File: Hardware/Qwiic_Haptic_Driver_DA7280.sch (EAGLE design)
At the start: 23 parts, among them J1 QWIIC_RIGHT_ANGLE, J2 QWIIC_RIGHT_ANGLE, M1 G1040003D_LRA_CASTELLATED, U1 HAPTIC_DRIVER_DA7280

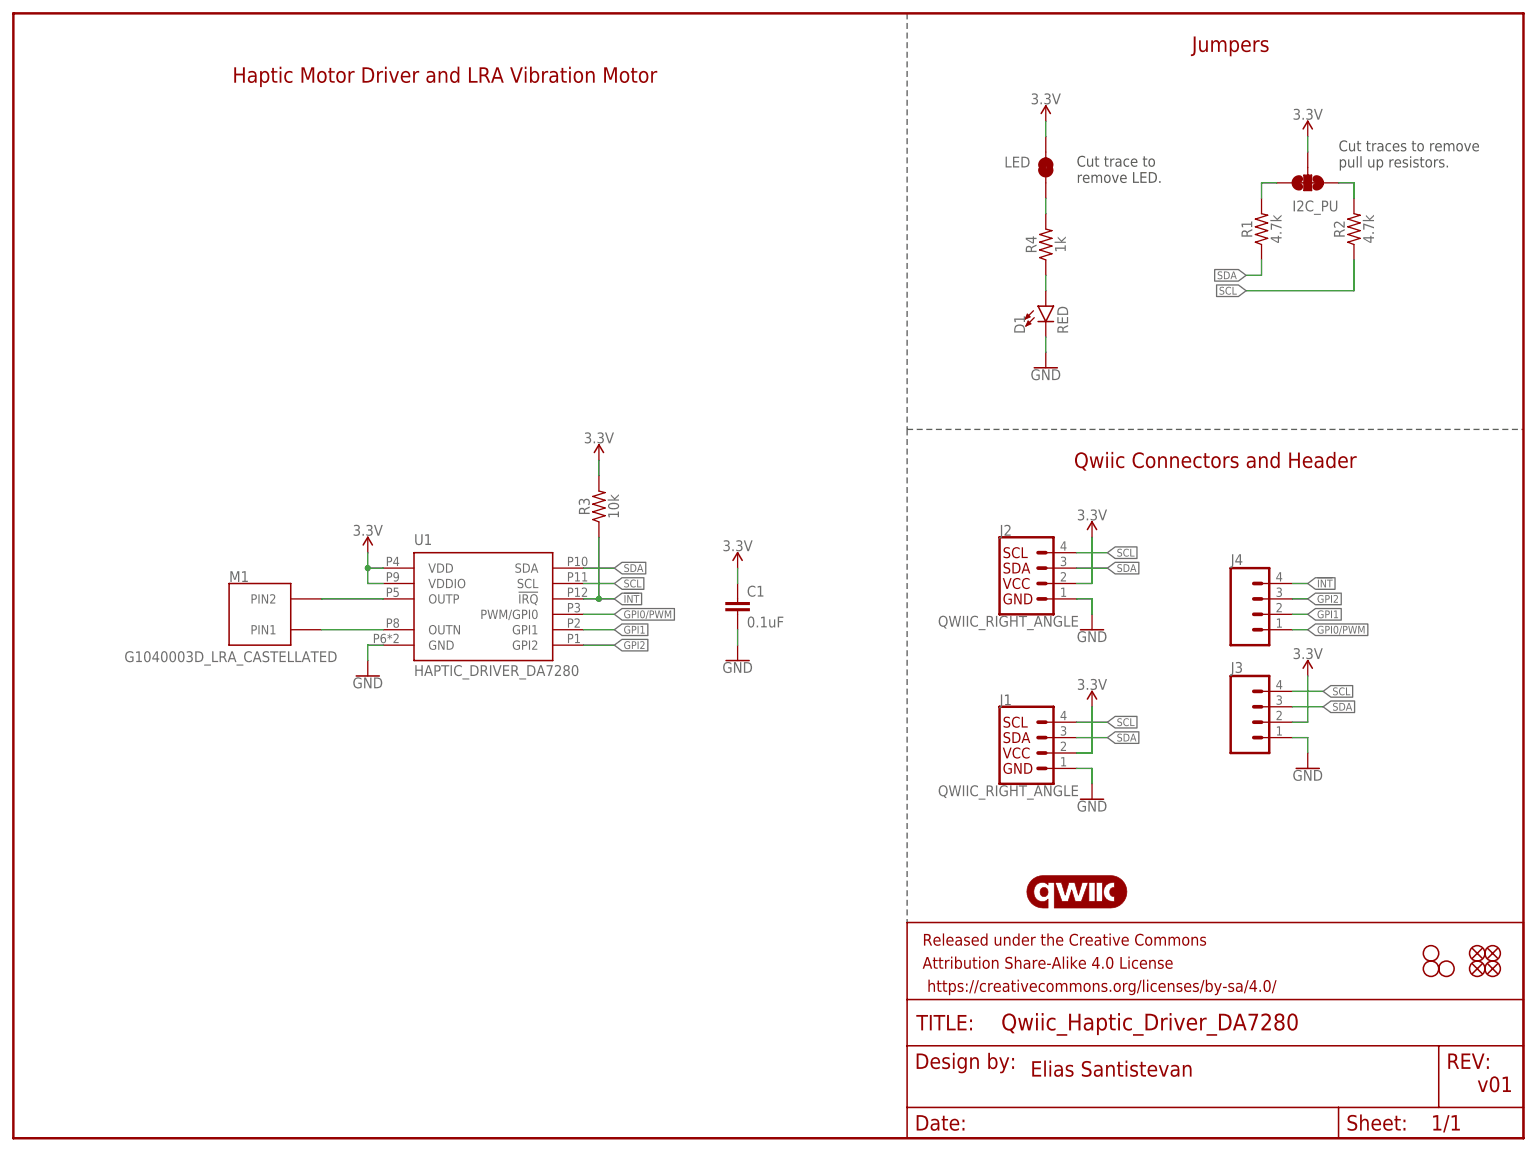
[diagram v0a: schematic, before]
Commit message: Flips the LRA motor 180, extends board to be 1.15 x 1 inches, adds 4.7iF decoupling capacitor
* Gerbers in repo are out of date
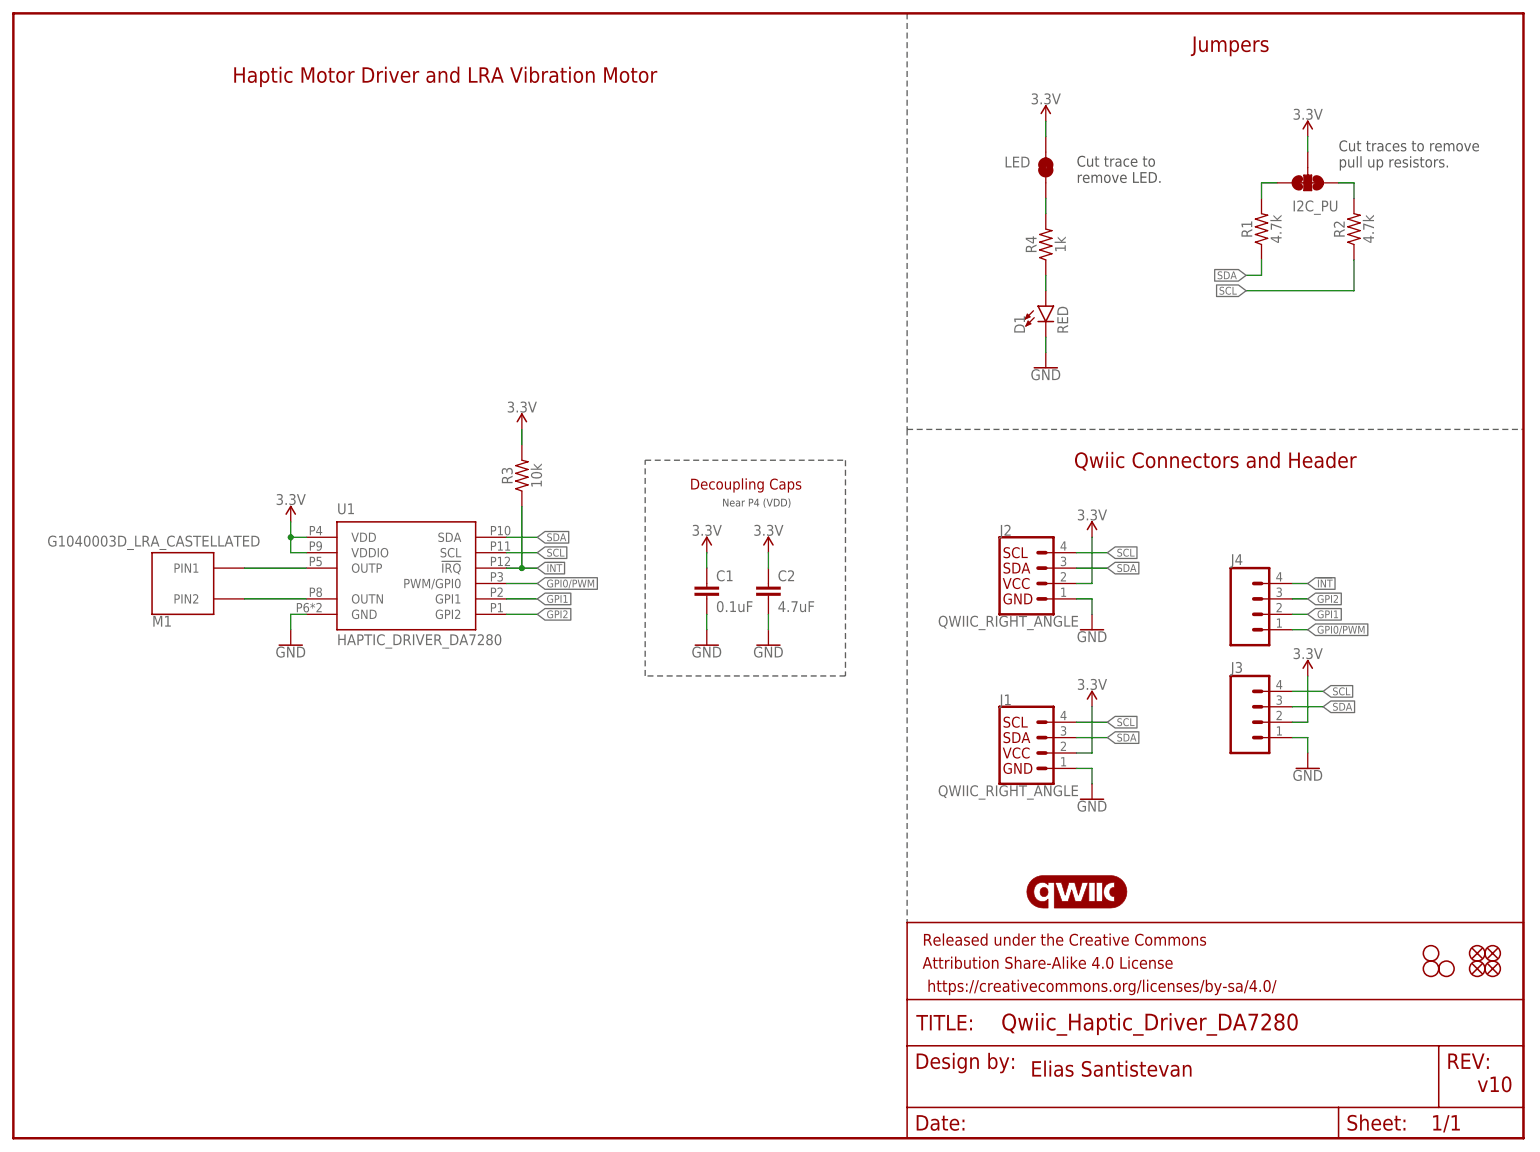
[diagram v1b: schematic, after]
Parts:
- added C2: 4.7uF, SparkFun-Capacitors:4.7UF-0603-6.3V-(10%)
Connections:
- net 3.3V: now also C2.1
- net GND: now also C2.2
- net N$5: now also U1.OUTP; no longer U1.OUTN
- net N$6: now also U1.OUTN; no longer U1.OUTP
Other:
- note added: "Decoupling Caps"
- note added: "Near P4 (VDD)"
- note added: "v10"
- note removed: "v01"
- moved on the sheet: C1, M1, R3, U1

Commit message: Adds a jumper and plated through hole for separate VDDIO supply, adds silk for VDD
* Changes power symbols to VDD and VDDIO in place of 3V3
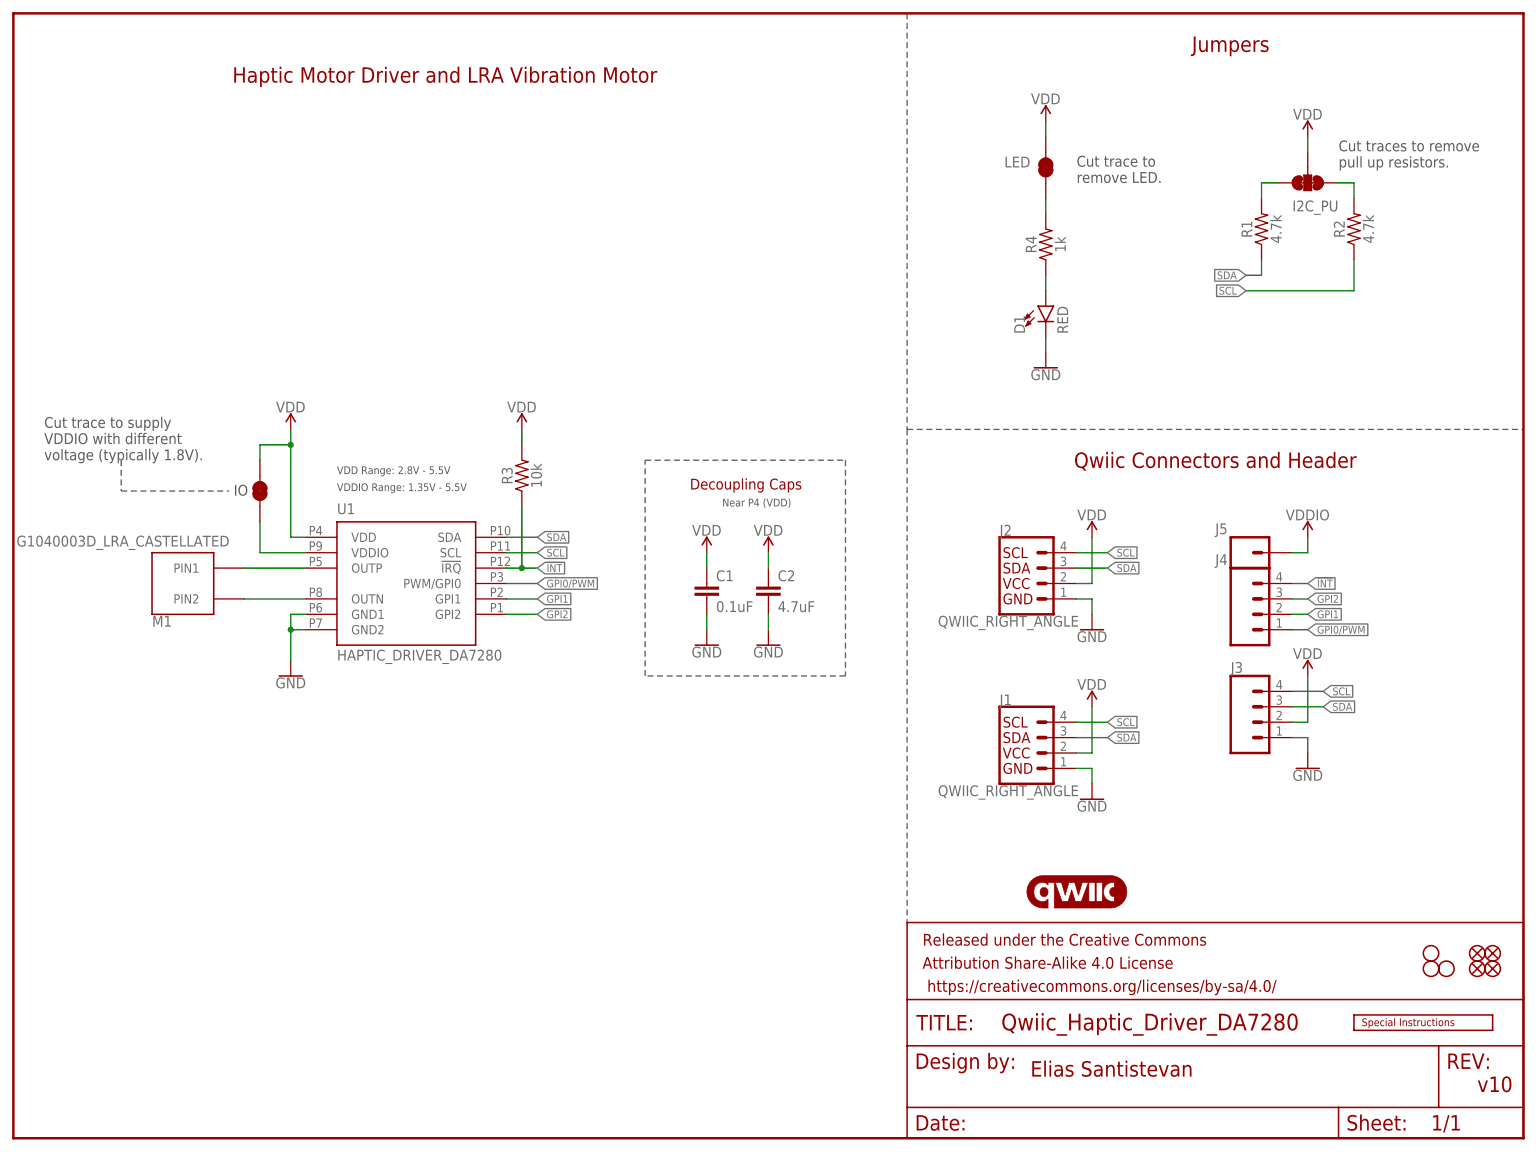
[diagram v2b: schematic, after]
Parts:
- added J5: (no value), SparkFun-Connectors:CONN_01PTH_NO_SILK_YES_STOP
- added JP2: LED, SparkFun-Jumpers:JUMPER-SMT_2_NC_TRACE_SILK
- added LOGO1: SPECIAL_INSTRUCTIONS-ORDERING, SparkFun-Aesthetics:SPECIAL_INSTRUCTIONS-ORDERING
- U$1: value QWIIC_LOGO_5MM -> QWIIC_LOGO_3MM; device SparkFun-Aesthetics:QWIIC_LOGO_5MM -> SparkFun-Aesthetics:QWIIC_LOGO_3MM
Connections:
- removed net 3.3V: C1.1, C2.1, J1.2, J2.2, J3.2, JP1.2, JP3.2, R3.2, U1.VDD, U1.VDDIO
- new net VDD: C1.1, C2.1, J1.2, J2.2, J3.2, JP1.2, JP2.2, JP3.2, R3.2, U1.VDD
- new net VDDIO: J5.1, JP2.1, U1.VDDIO
- net GND: now also U1.GND1, U1.GND2; no longer U1.GND
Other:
- note added: "Cut trace to supply VDDIO with different voltage (typically 1.8V)."
- note added: "IO"
- note added: "VDD Range: 2.8V - 5.5V"
- note added: "VDDIO Range: 1.35V - 5.5V"

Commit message: Adds Jumpers for separating VDDIO from VDD and Qwiic bus voltage from the board
* Updates measures
* Adds OSHW and SparkFun logo to board
* Adds text to jumpers in the schematic
* Updates symbol to use short legs
* Adds VDD and VDDIO range
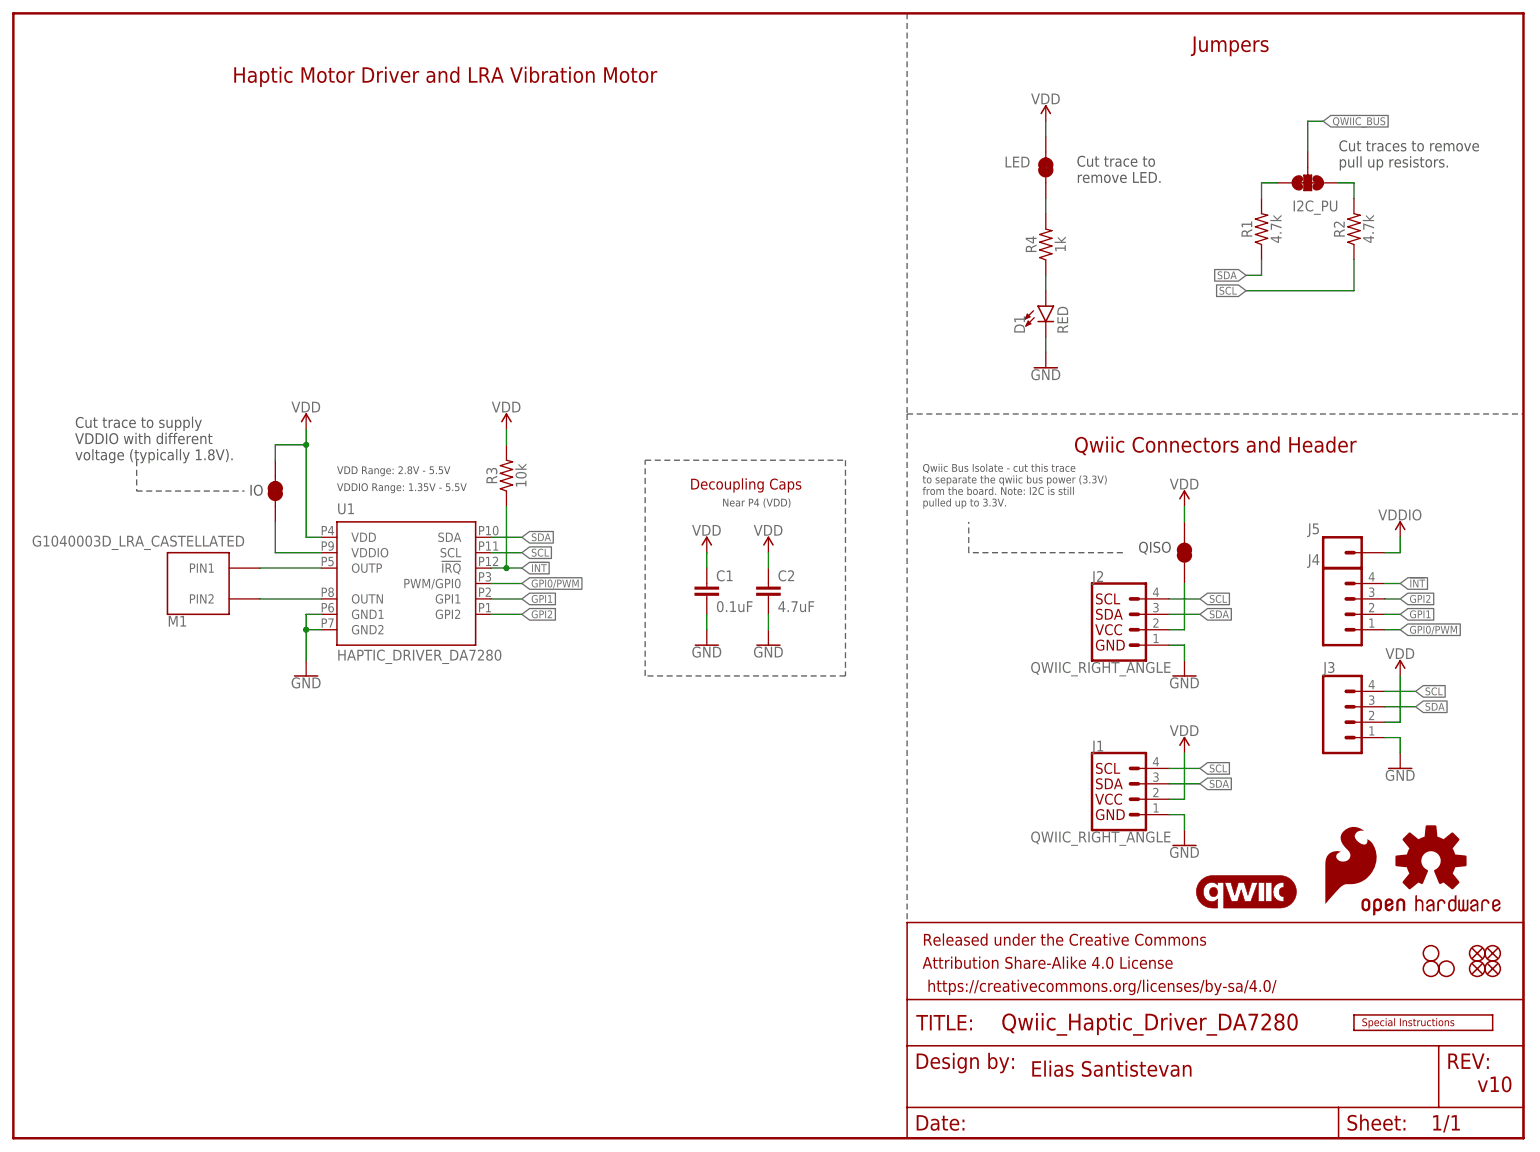
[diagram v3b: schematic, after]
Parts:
- added JP4: LED, SparkFun-Jumpers:JUMPER-SMT_2_NC_TRACE_SILK
- added LOGO2: OSHW-LOGOS, SparkFun-Aesthetics:OSHW-LOGOS
- added LOGO4: SFE_LOGO_FLAME.1_INCH, SparkFun-Aesthetics:SFE_LOGO_FLAME.1_INCH
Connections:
- new net QWIIC_BUS: J2.2, JP3.2, JP4.1
- net VDD: now also JP4.2; no longer J2.2, JP3.2
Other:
- note added: "QISO"
- note added: "Qwiic Bus Isolate - cut this trace to separate the qwiic bus power (3.3V) from the board. Note: I2C is still pulled up to 3.3V."
- moved on the sheet: J1, J2, J3, J4, J5, M1, R3
